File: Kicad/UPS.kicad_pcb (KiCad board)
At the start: 2 copper layers, 13 parts, among them J2 Conn_02x20_Odd_Even, J3 GET_UP_SERVO_RIGHT, J4 Conn_01x02_Male, J5 Y_HEAD_PAN, J6 Y_HEAD_PAN, J7 X_CLAW, J8 Y_CLAWN, SW1 SW_Push

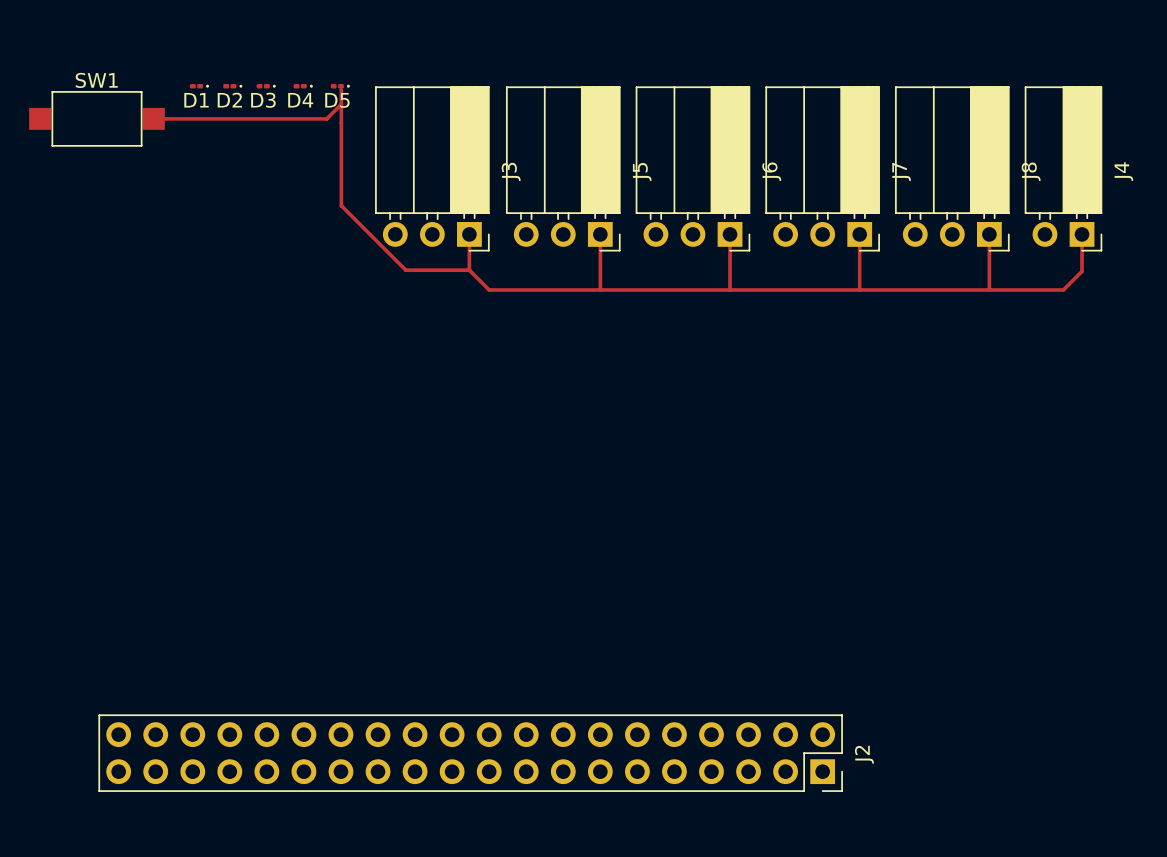
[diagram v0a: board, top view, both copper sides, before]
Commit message: Add usb footprint
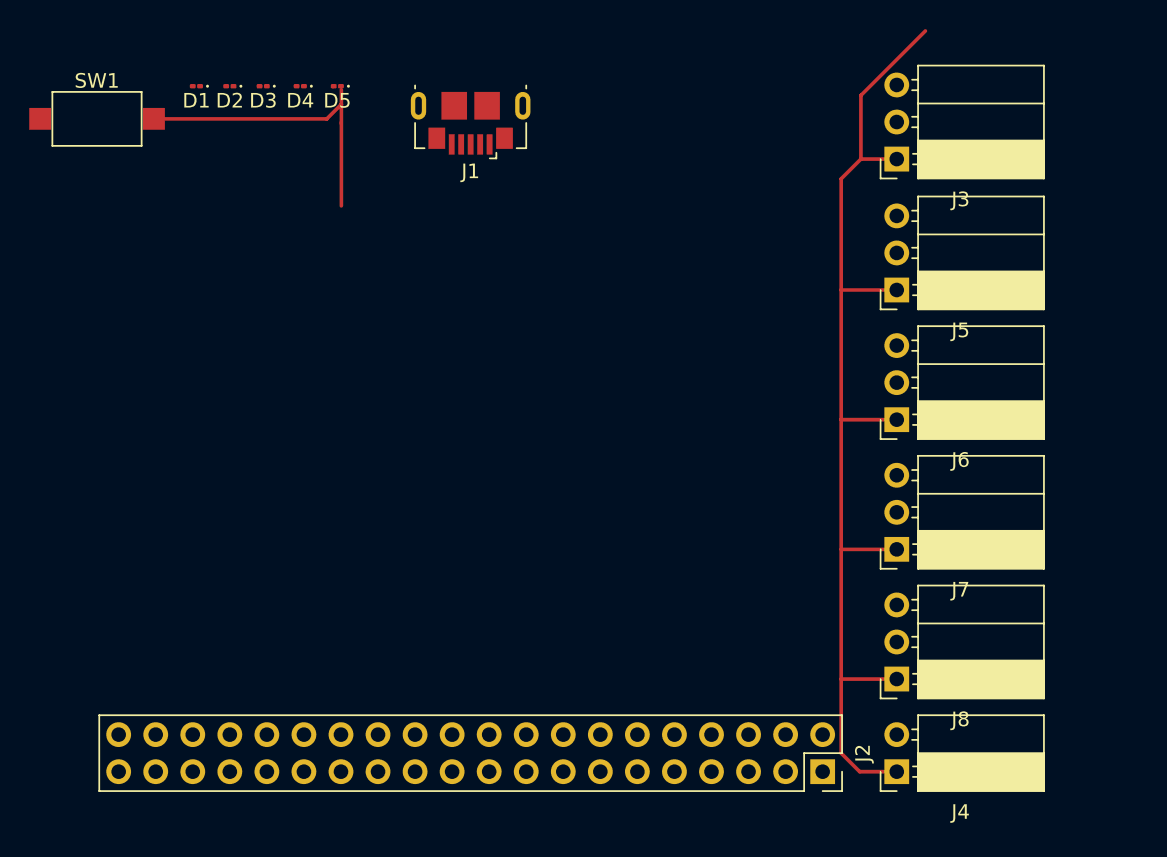
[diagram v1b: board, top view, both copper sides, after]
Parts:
- added J1: USB_B_Micro, Connector_USB:USB_Micro-B_GCT_USB3076-30-A, F.Cu at (148.6, 62.2)
- moved J4 39.0 mm to (177.8, 106.7), turned to 180 degrees
- moved J8 31.1 mm to (177.8, 100.3), turned to 180 degrees
- moved J3 29.7 mm to (177.8, 64.7), turned to 180 degrees
- moved J7 21.7 mm to (177.8, 91.4), turned to 180 degrees
- moved J5 20.7 mm to (177.8, 73.7), turned to 180 degrees
- moved J6 17.1 mm to (177.8, 82.5), turned to 180 degrees
